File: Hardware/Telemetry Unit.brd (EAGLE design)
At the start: 50.8 x 63.5 mm, 55 parts, among them IC1 MEGA128-A, IC2 FT232RL, J2 503182-1852, J3 10118193-0001LF, Q1 10MHz, U1 MPL3115A2, U2 AP65111A, U3 LSM6DS3

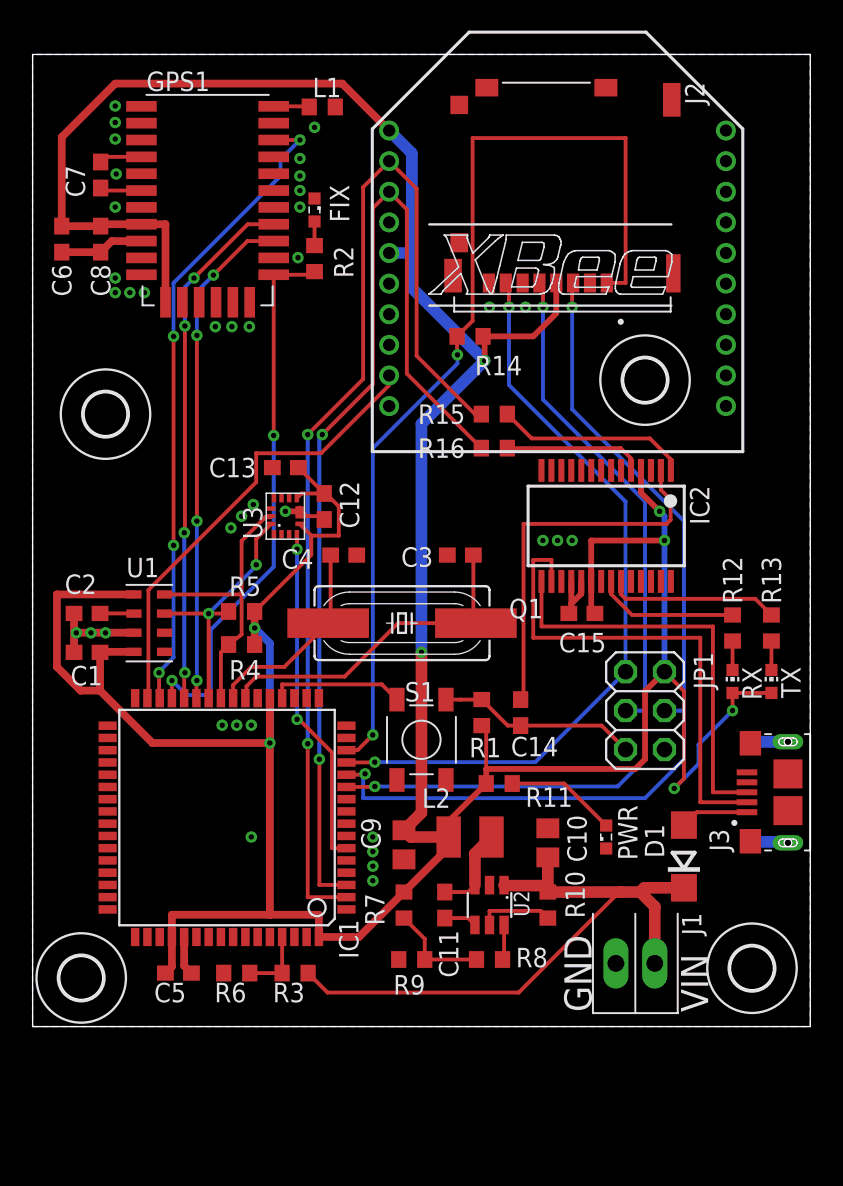
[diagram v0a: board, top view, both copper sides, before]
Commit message: Fix USB port nonsense/xBee logo
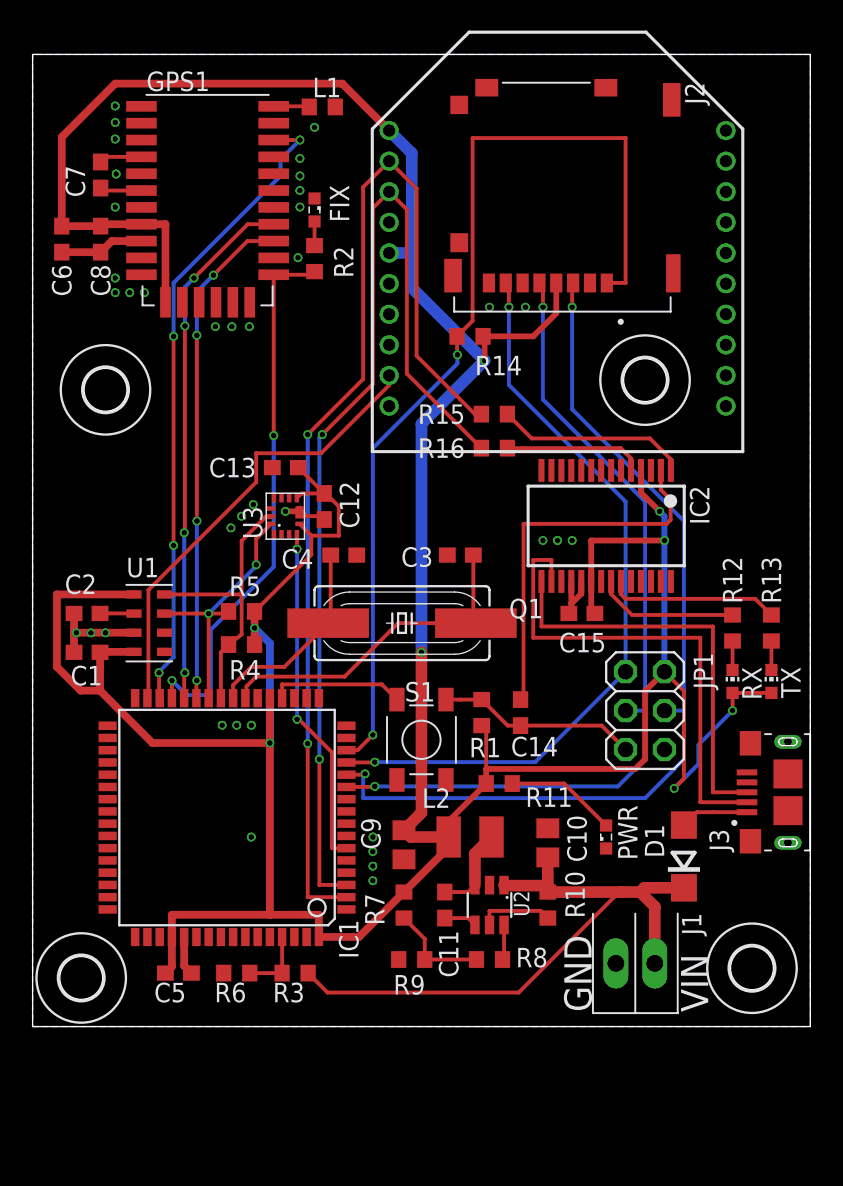
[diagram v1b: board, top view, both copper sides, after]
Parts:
- XB1: device maxstream:XBEE -> TrackerPeripherals:XBEE
- moved U$1 1.59 mm to (4.76, 41.6)
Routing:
- net GND: track 26.7 -> 22.5 mm

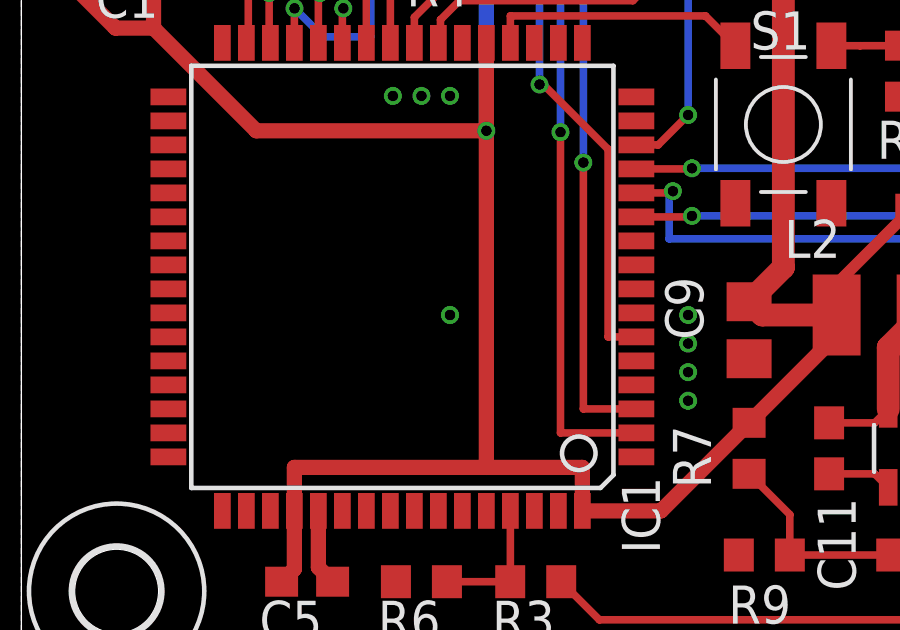
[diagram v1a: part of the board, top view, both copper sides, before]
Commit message: Removed via
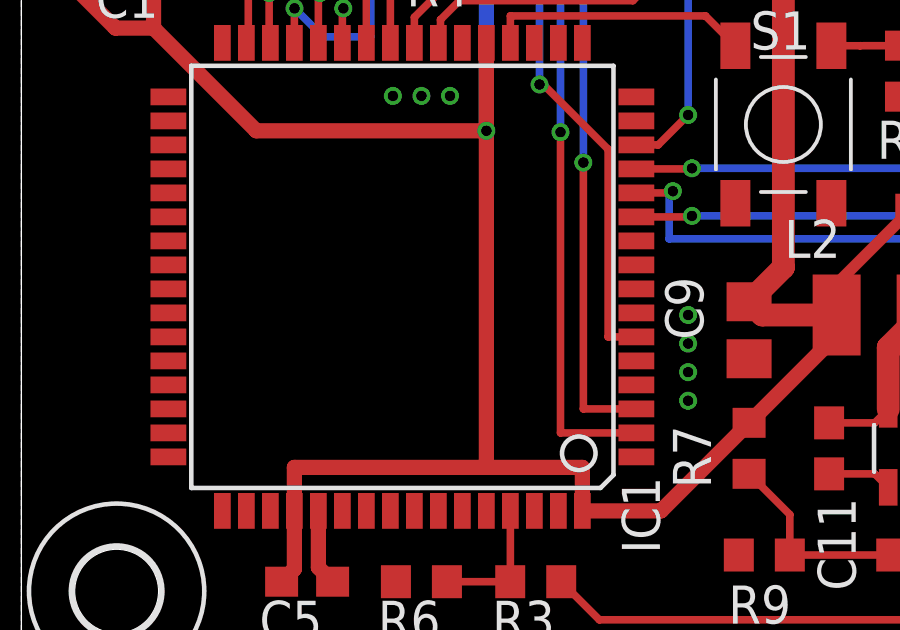
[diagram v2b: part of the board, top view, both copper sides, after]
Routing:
- net GND: vias 38 -> 37
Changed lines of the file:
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@@
 <via x="29.845" y="46.99" extent="1-16" drill="0.35"/>
 <via x="32.1945" y="46.99" extent="1-16" drill="0.35"/>
-<via x="14.2875" y="12.3825" extent="1-16" drill="0.35"/>
 <contactref element="S1" pad="P$1"/>
 </signal>

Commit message: Added fuse to usb
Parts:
- added F1: MF-MSMF050-2, MF-MSMF050-2:FUSM1812X02
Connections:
- new net N$22: F1.1, J3.1
- net V_USB: now also F1.2; no longer J3.1
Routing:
- net N$22: track 0.00 -> 5.92 mm
- net V_USB: track 4.47 -> 5.83 mm
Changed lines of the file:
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@@
 <?xml version="1.0" encoding="utf-8"?>
 <!DOCTYPE eagle SYSTEM "eagle.dtd">
-<eagle version="9.2.2">
+<eagle version="9.3.0">
 <drawing>
 <settings>
@@
 <attribute name="VALUE" x="30.7975" y="39.6875" size="1.27" layer="27" rot="R180"/>
 </element>
+<element name="F1" library="MF-MSMF050-2" package="FUSM1812X02" value="MF-MSMF050-2" x="46.99" y="9.2075" smashed="yes" rot="R180">
+<attribute name="AVAILABILITY" value="Unavailable" x="46.99" y="9.2075" size="1.778" layer="27" rot="R180" display="off"/>
+<attribute name="DESCRIPTION" value=" PTC Resettable Fuse 0.5A_hold_ 1A_trip_ 15V 100A 0.8W 0.15s 0.15Ohm SMD Solder Pad 1812 T/R " x="46.99" y="9.2075" size="1.778" layer="27" rot="R180" display="off"/>
+<attribute name="MF" value="Bourns" x="46.99" y="9.2075" size="1.778" layer="27" rot="R180" display="off"/>
+<attribute name="MP" value="MF-MSMF050-2" x="46.99" y="9.2075" size="1.778" layer="27" rot="R180" display="off"/>
+<attribute name="NAME" x="48.89605" y="6.666109375" size="1.2707" layer="25" rot="R180"/>
+<attribute name="PACKAGE" value="1812 Bourns" x="46.99" y="9.2075" size="1.778" layer="27" rot="R180" display="off"/>
+<attribute name="PRICE" value="None" x="46.99" y="9.2075" size="1.778" layer="27" rot="R180" display="off"/>
+<attribute name="VALUE" x="48.89841875" y="13.02435" size="1.27228125" layer="27" rot="R180"/>
+</element>
 </elements>
 <signals>
@@
 </signal>
 <signal name="V_USB">
-<contactref element="J3" pad="1"/>
 <contactref element="D1" pad="A"/>
-<wire x1="43.386" y1="14.0035" x2="42.545" y2="13.1625" width="0.254" layer="1"/>
-<wire x1="46.6645" y1="14.0035" x2="44.45" y2="14.0035" width="0.254" layer="1"/>
-<wire x1="44.45" y1="14.0035" x2="43.386" y2="14.0035" width="0.254" layer="1"/>
+<contactref element="F1" pad="2"/>
+<wire x1="45.04" y1="9.2075" x2="44.1325" y2="10.115" width="0.381" layer="1"/>
+<wire x1="44.1325" y1="10.115" x2="44.1325" y2="13.0175" width="0.381" layer="1"/>
+<wire x1="44.1325" y1="13.0175" x2="43.9875" y2="13.1625" width="0.381" layer="1"/>
+<wire x1="43.9875" y1="13.1625" x2="42.545" y2="13.1625" width="0.381" layer="1"/>
 </signal>
 <signal name="N$11">
@@
 <wire x1="38.4175" y1="37.7825" x2="39.09" y2="37.11" width="0.254" layer="1"/>
 </signal>
+<signal name="N$22">
+<contactref element="J3" pad="1"/>
+<contactref element="F1" pad="1"/>
+<wire x1="46.6645" y1="14.0035" x2="47.4216" y2="13.2464" width="0.381" layer="1"/>
+<wire x1="47.4216" y1="13.2464" x2="47.73153125" y2="13.2464" width="0.381" layer="1"/>
+<wire x1="48.94" y1="10.83166875" x2="48.94" y2="9.2075" width="0.381" layer="1"/>
+<wire x1="48.0966" y1="11.67506875" x2="48.94" y2="10.83166875" width="0.381" layer="1"/>
+<wire x1="47.73153125" y1="13.2464" x2="48.0966" y2="12.88133125" width="0.381" layer="1"/>
+<wire x1="48.0966" y1="12.88133125" x2="48.0966" y2="11.67506875" width="0.381" layer="1"/>
+</signal>
 </signals>
 <mfgpreviewcolors>
@@
 <mfgpreviewcolor name="substratecolor" color="0xFF786E46"/>
 </mfgpreviewcolors>
-<errors>
-</errors>
 </board>
 </drawing>

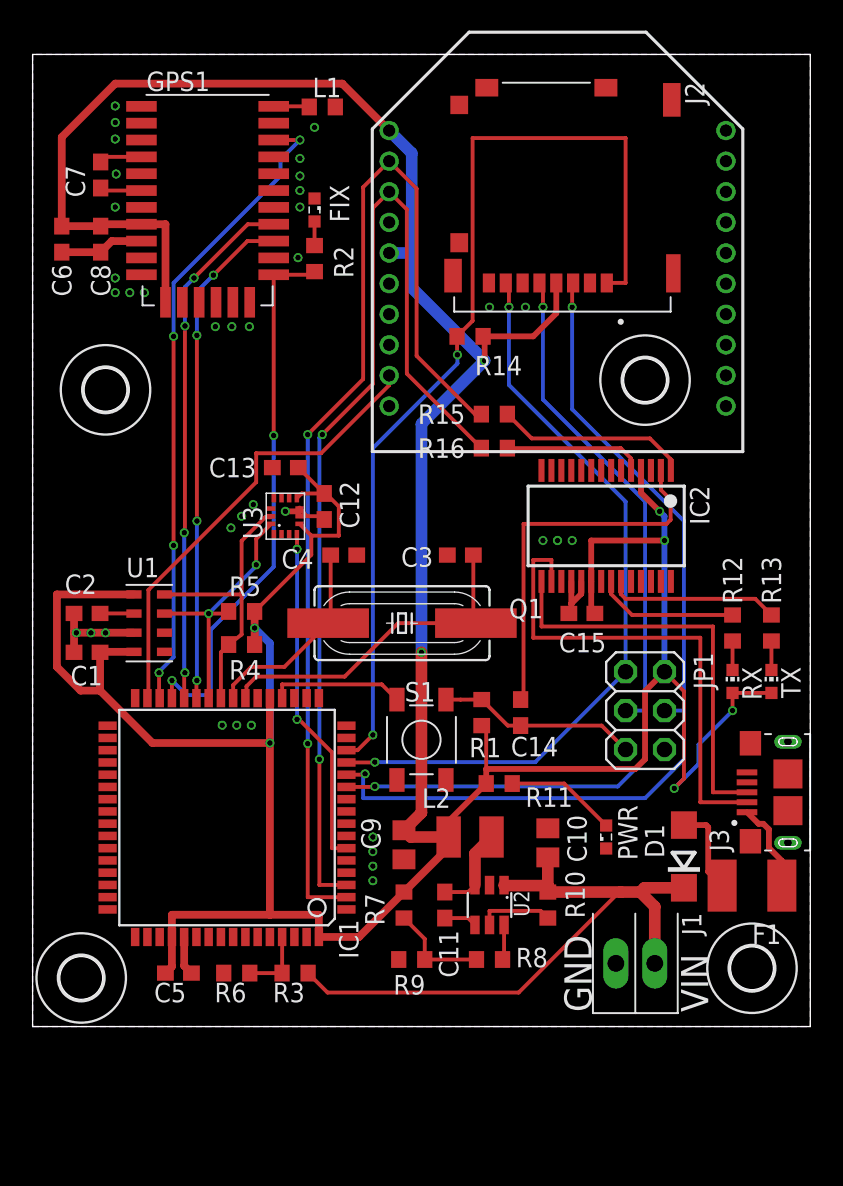
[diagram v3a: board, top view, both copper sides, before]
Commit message: Consolidated resistors and capacitors
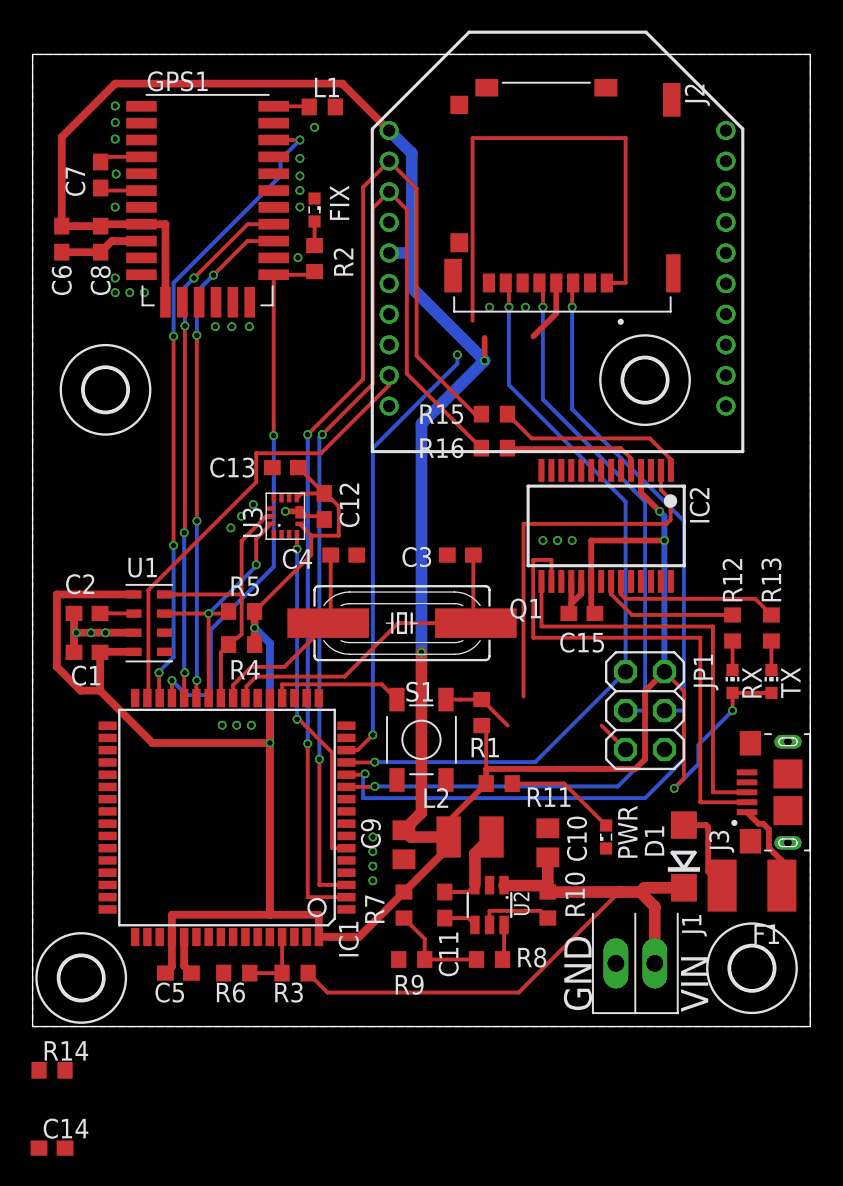
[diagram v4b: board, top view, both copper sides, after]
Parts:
- C14: value 100nF -> 100n; device rcl:C0603 -> resistor:C0603
- R14: device rcl:R0603 -> resistor:R0603
- moved R14 55.2 mm to (1.27, -2.86)
- moved C14 41.8 mm to (1.27, -7.94), turned to 0 degrees
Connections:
- net +3V3: now also R14.1; no longer R14.2
- net CS_SD: now also R14.2; no longer R14.1
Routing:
- net RST2: track 13.1 -> 6.95 mm
- net +3V3: track 271.6 -> 268.2 mm
- net CS_SD: track 64.5 -> 61.9 mm
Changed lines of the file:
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@@
 <attribute name="VALUE" x="41.3649" y="33.3825" size="1.27" layer="27" rot="R180"/>
-</element>
-<element name="C14" library="rcl" library_urn="urn:adsk.eagle:library:334" package="C0603" package3d_urn="urn:adsk.eagle:package:23616/2" value="100nF" x="31.877" y="20.5105" smashed="yes" rot="R270">
-<attribute name="NAME" x="31.242" y="17.653" size="1.27" layer="25"/>
-<attribute name="SPICEPREFIX" value="C" x="31.877" y="20.5105" size="1.778" layer="27" rot="R270" display="off"/>
-<attribute name="VALUE" x="29.972" y="21.1455" size="1.27" layer="27" rot="R270"/>
 </element>
 <element name="R12" library="rcl" library_urn="urn:adsk.eagle:library:334" package="R0603" package3d_urn="urn:adsk.eagle:package:23555/2" value="1k" x="45.72" y="26.035" smashed="yes" rot="R90">
@@
 <attribute name="NAME" x="48.895" y="23.495" size="1.27" layer="25" rot="R270"/>
 <attribute name="VALUE" x="50.165" y="21.9075" size="1.27" layer="27" rot="R90"/>
-</element>
-<element name="R14" library="rcl" library_urn="urn:adsk.eagle:library:334" package="R0603" package3d_urn="urn:adsk.eagle:package:23555/2" value="10k" x="28.575" y="45.085" smashed="yes">
-<attribute name="NAME" x="28.8925" y="42.545" size="1.27" layer="25"/>
-<attribute name="SPICEPREFIX" value="R" x="28.575" y="45.085" size="1.778" layer="27" display="off"/>
-<attribute name="VALUE" x="27.94" y="43.18" size="1.27" layer="27"/>
 </element>
 <element name="JP1" library="pinhead" library_urn="urn:adsk.eagle:library:325" package="2X03" package3d_urn="urn:adsk.eagle:package:22462/2" value="" x="40.005" y="20.6375" smashed="yes" rot="R270">
@@
 <attribute name="PRICE" value="None" x="46.99" y="9.2075" size="1.778" layer="27" rot="R180" display="off"/>
 <attribute name="VALUE" x="48.89841875" y="13.02435" size="1.27228125" layer="27" rot="R180"/>
+</element>
+<element name="R14" library="resistor" library_urn="urn:adsk.eagle:library:348" package="R0603" package3d_urn="urn:adsk.eagle:package:23555/3" value="10k" x="1.27" y="-2.8575" smashed="yes">
+<attribute name="NAME" x="0.635" y="-2.2225" size="1.27" layer="25"/>
+<attribute name="VALUE" x="0.635" y="-4.7625" size="1.27" layer="27"/>
+</element>
+<element name="C14" library="resistor" library_urn="urn:adsk.eagle:library:348" package="C0603" package3d_urn="urn:adsk.eagle:package:23616/2" value="100n" x="1.27" y="-7.9375" smashed="yes">
+<attribute name="NAME" x="0.635" y="-7.3025" size="1.27" layer="25"/>
+<attribute name="VALUE" x="0.635" y="-9.8425" size="1.27" layer="27"/>
 </element>
 </elements>
@@
 <wire x1="4.436" y1="24.4775" x2="4.406" y2="24.4475" width="0.254" layer="1"/>
 <contactref element="J2" pad="4"/>
-<contactref element="R14" pad="2"/>
 <contactref element="XB1" pad="5"/>
 <contactref element="XB1" pad="1"/>
@@
 <wire x1="23.29" y1="50.53" x2="24.7175" y2="50.53" width="0.762" layer="16"/>
 <wire x1="24.7175" y1="50.53" x2="24.765" y2="50.4825" width="0.762" layer="16"/>
-<wire x1="29.425" y1="45.085" x2="29.5275" y2="44.9825" width="0.254" layer="1"/>
 <wire x1="29.5275" y1="44.9825" x2="29.5275" y2="43.4975" width="0.381" layer="1"/>
 <via x="29.5275" y="43.4975" extent="1-16" drill="0.35"/>
@@
 <wire x1="40.005" y1="17.4625" x2="39.37" y2="16.8275" width="0.381" layer="1"/>
 <wire x1="39.37" y1="16.8275" x2="29.63" y2="16.8275" width="0.381" layer="1"/>
-<wire x1="29.425" y1="45.085" x2="32.7025" y2="45.085" width="0.381" layer="1"/>
 <wire x1="34.2075" y1="46.59" x2="34.2075" y2="48.5725" width="0.381" layer="1"/>
 <wire x1="32.7025" y1="45.085" x2="34.2075" y2="46.59" width="0.381" layer="1"/>
@@
 <wire x1="36.49" y1="27.225" x2="36.49" y2="29.0775" width="0.381" layer="1"/>
 <via x="41.91" y="15.5575" extent="1-16" drill="0.35"/>
+<contactref element="R14" pad="1"/>
+<wire x1="29.5275" y1="44.9825" x2="32.7025" y2="45.085" width="0" layer="19" extent="1-1"/>
+<wire x1="0.42" y1="-2.8575" x2="8.675" y2="3.4925" width="0" layer="19" extent="1-1"/>
 </signal>
 <signal name="GND">
@@
 <wire x1="27" y1="21.3575" x2="27.9575" y2="21.3575" width="0.254" layer="1"/>
 <wire x1="27.9575" y1="21.3575" x2="29.337" y2="21.3605" width="0.254" layer="1"/>
-<contactref element="C14" pad="2"/>
-<wire x1="31.877" y1="19.6605" x2="31.037" y2="19.6605" width="0.254" layer="1"/>
 <wire x1="31.037" y1="19.6605" x2="29.337" y2="21.3605" width="0.254" layer="1"/>
 <contactref element="JP1" pad="5"/>
-<wire x1="31.877" y1="19.6605" x2="37.172" y2="19.6605" width="0.254" layer="1"/>
 <wire x1="37.172" y1="19.6605" x2="38.735" y2="18.0975" width="0.254" layer="1"/>
+<contactref element="C14" pad="2"/>
+<wire x1="31.037" y1="19.6605" x2="37.172" y2="19.6605" width="0" layer="19" extent="1-1"/>
+<wire x1="2.12" y1="-7.9375" x2="27" y2="21.3575" width="0" layer="19" extent="1-1"/>
 </signal>
 <signal name="CS_SD">
 <contactref element="IC1" pad="14"/>
-<contactref element="R14" pad="1"/>
 <contactref element="J2" pad="1"/>
 <wire x1="20.5" y1="18.0525" x2="21.2275" y2="18.0525" width="0.254" layer="1"/>
@@
 <via x="27.7495" y="43.8785" extent="1-16" drill="0.35"/>
 <wire x1="27.7495" y1="43.8785" x2="27.725" y2="43.903" width="0.254" layer="1"/>
-<wire x1="27.725" y1="43.903" x2="27.725" y2="45.085" width="0.254" layer="1"/>
 <wire x1="38.735" y1="48.5775" x2="38.735" y2="58.0375" width="0.254" layer="1"/>
 <wire x1="38.735" y1="58.0375" x2="28.741" y2="58.0375" width="0.254" layer="1"/>
 <wire x1="28.741" y1="58.0375" x2="28.741" y2="46.101" width="0.254" layer="1"/>
-<wire x1="28.741" y1="46.101" x2="27.725" y2="45.085" width="0.254" layer="1"/>
 <wire x1="37.5075" y1="48.5725" x2="37.5125" y2="48.5775" width="0.254" layer="1"/>
 <wire x1="37.5125" y1="48.5775" x2="38.735" y2="48.5775" width="0.254" layer="1"/>
+<contactref element="R14" pad="2"/>
+<wire x1="27.725" y1="43.903" x2="28.741" y2="46.101" width="0" layer="19" extent="1-1"/>
+<wire x1="2.12" y1="-2.8575" x2="20.5" y2="18.0525" width="0" layer="19" extent="1-1"/>
 </signal>
 <signal name="V_USB">
@@
 </signal>
 <signal name="N$16">
-<contactref element="C14" pad="1"/>
 <contactref element="IC2" pad="2"/>
-<wire x1="32.0675" y1="21.551" x2="31.877" y2="21.3605" width="0.254" layer="1"/>
 <wire x1="41.675" y1="34.4225" x2="41.04" y2="35.0575" width="0.254" layer="1"/>
 <wire x1="41.04" y1="36.3275" x2="41.04" y2="35.0575" width="0.254" layer="1"/>
@@
 <wire x1="41.675" y1="33.1025" x2="41.4075" y2="32.835" width="0.254" layer="1"/>
 <wire x1="41.4075" y1="32.835" x2="32.0675" y2="32.835" width="0.254" layer="1"/>
+<contactref element="C14" pad="1"/>
+<wire x1="0.42" y1="-7.9375" x2="32.0675" y2="21.551" width="0" layer="19" extent="1-1"/>
 </signal>
 <signal name="N$15">
